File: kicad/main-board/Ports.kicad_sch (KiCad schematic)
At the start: 25 parts, among them J43 USB_A_Stacked, J44 USB_A, J45 USB_C_Receptacle, J46 THD-02-R, J47 USB3_A, J48 HDMI_A, J49 HDMI_C_1.3, U22 C2684433, U23 RT9742SNGV, U3 CM5108064B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

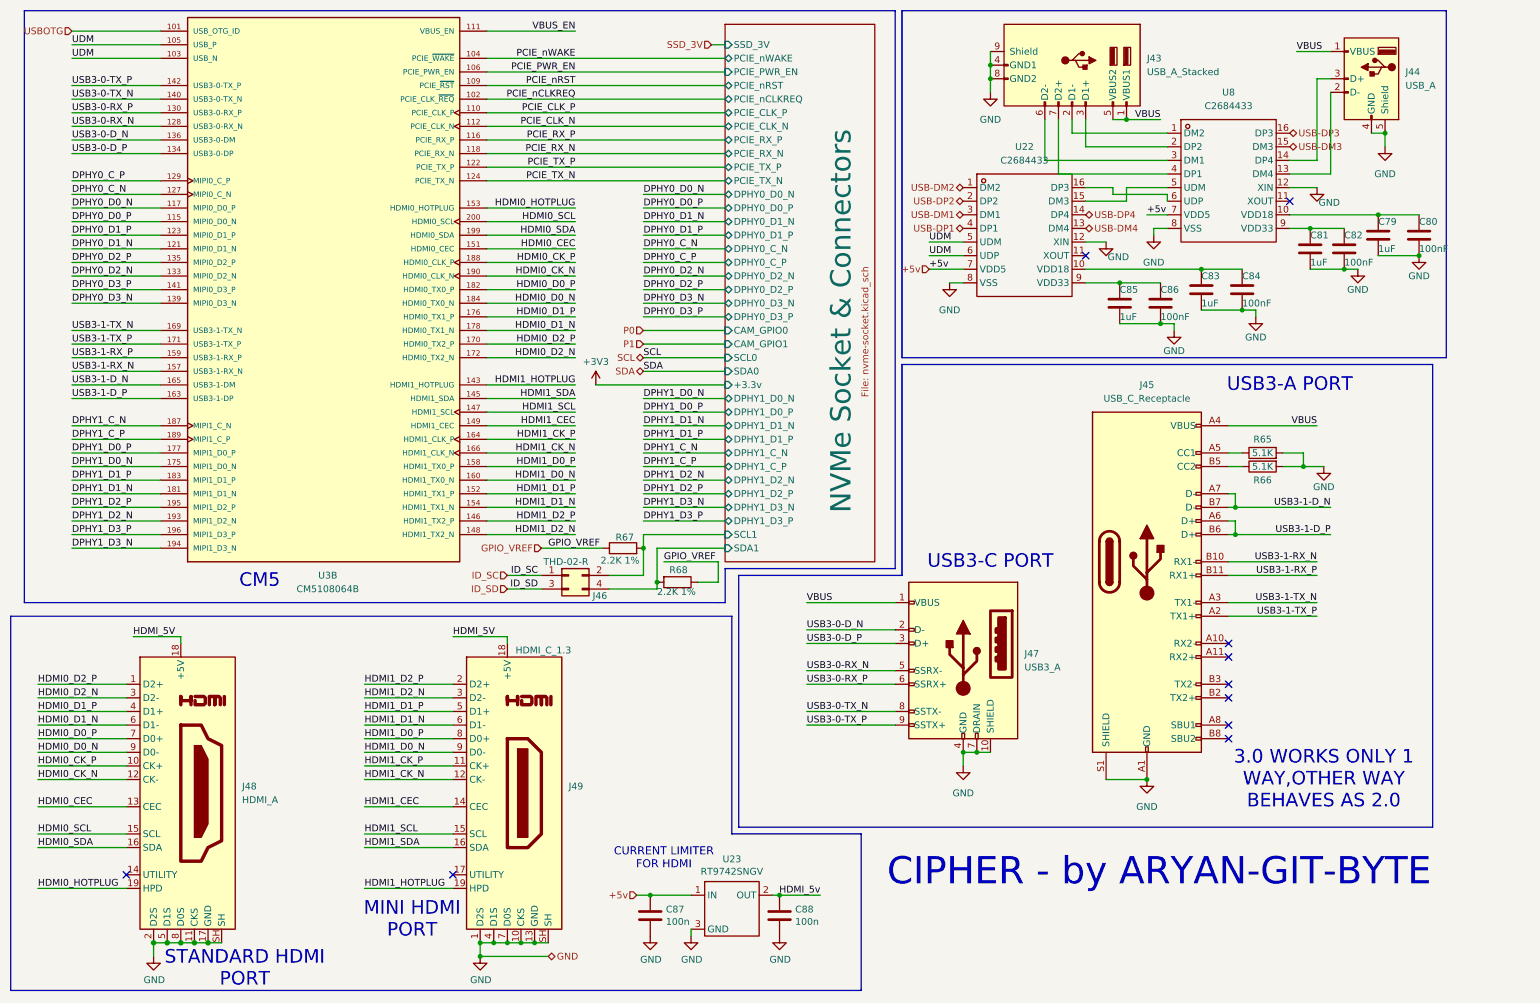
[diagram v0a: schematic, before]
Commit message: migrating kicad 9 to 10
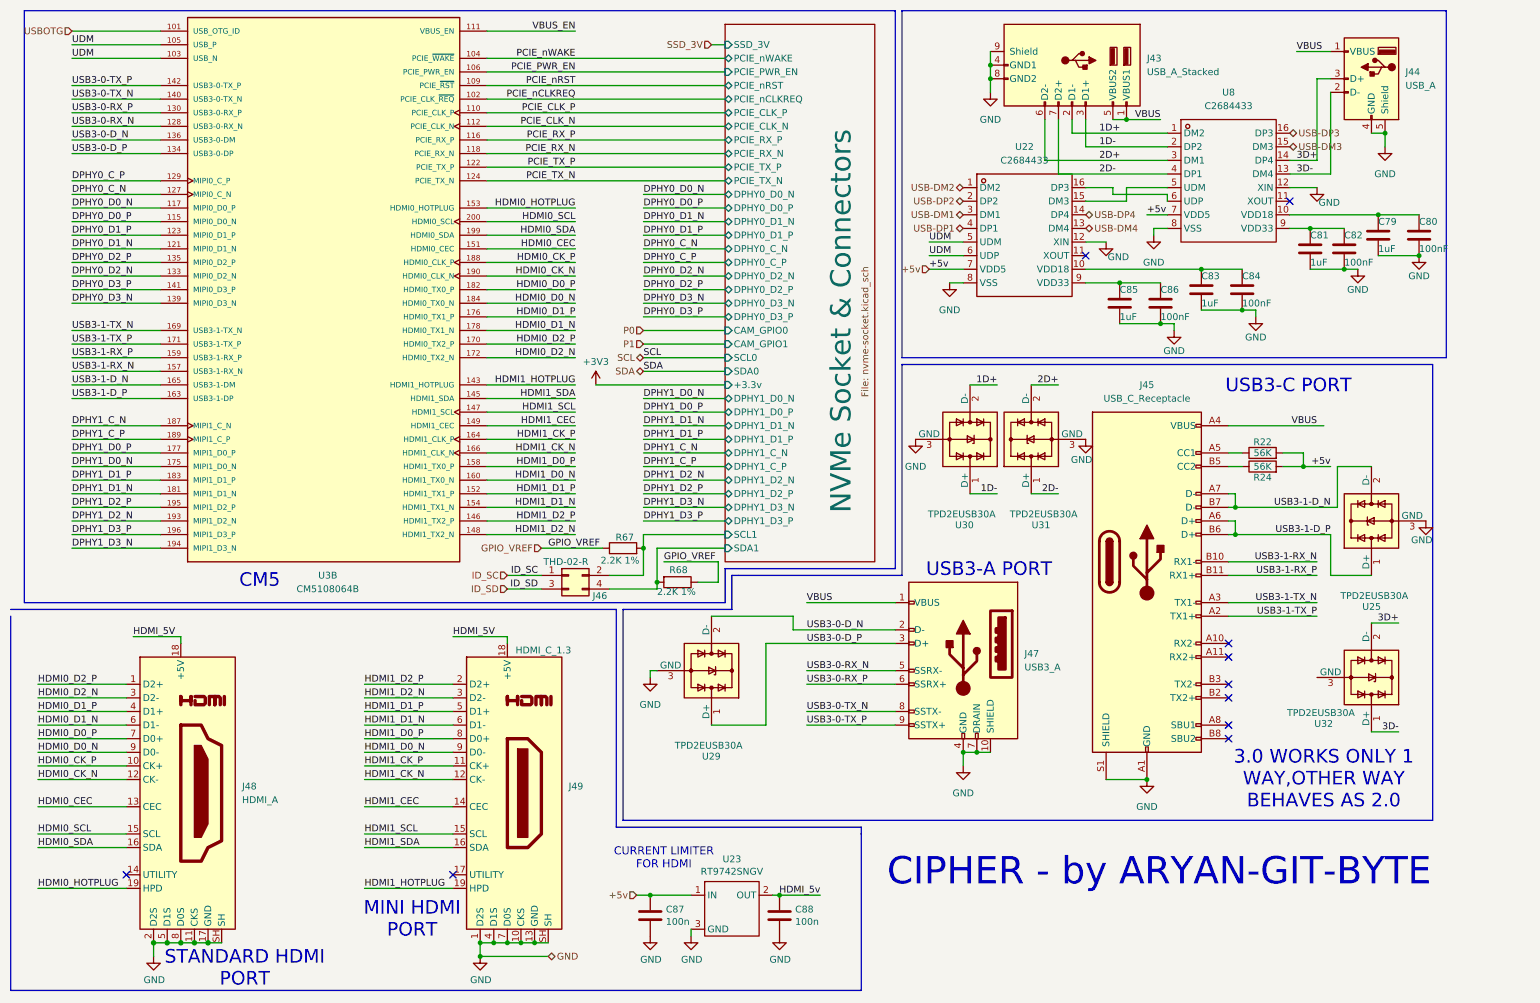
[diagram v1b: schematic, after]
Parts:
- removed R65, R66: 5.1K, symbol Device:R
- added R22, R24: 56K, symbol Device:R
- added U25, U29, U30, U31, U32: TPD2EUSB30A, Package_TO_SOT_SMD:Texas_DRT-3, symbol Power_Protection:TPD2EUSB30A
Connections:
- net +5v: now also R22.2, R24.2
- net GND: now also U25.3 (GND), U29.3 (GND), U30.3 (GND), U31.3 (GND)
- net USB3-0-D_N: now also U29.2 (D-)
- net USB3-0-D_P: now also U29.1 (D+)
- net USB3-1-D_N: now also U25.2 (D-)
- net USB3-1-D_P: now also U25.1 (D+)
- net 1D+: now reaches J43.2 (D1-), U8.1 (DM2)
- net 1D+: now also U30.2 (D-)
- net 3D-: now reaches J44.2 (D-), U8.13 (DM4)
- net 3D-: now also U32.1 (D+)
- net 3D+: now reaches J44.3 (D+), U8.14 (DP4)
- net 3D+: now also U32.2 (D-)
- net 1D-: now reaches J43.3 (D1+), U8.2 (DP2)
- net 1D-: now also U30.1 (D+)
- net 2D+: now reaches J43.6 (D2-), U8.3 (DM1)
- net 2D+: now also U31.2 (D-)
- net 2D-: now reaches J43.7 (D2+), U8.4 (DP1)
- net 2D-: now also U31.1 (D+)
- net at J45.B5 (CC2): now also R24.1
- net at J45.A5 (CC1): now also R22.1
